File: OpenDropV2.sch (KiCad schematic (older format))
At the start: 195 parts, among them J1 DC_JACK, P1 CONN_01X01, P2 CONN_01X01, P3 CONN_01X01, P4 CONN_01X01, P5 CONN_01X01, Q1 BSS138, Q2 BSS138, Q3 BSS138, SW1 SW_PUSH, SW2 SW_PUSH, SW3 SW_PUSH, SW4 SW_PUSH, SW5 SPST, T1 IRF 840S, U1 MAX1771ESA, U2 HV507, U3 ARDUINO_MICRO, U4 HV507, U5 ESP8266_SMD

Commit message: started with corrections for V2.1
work in progress
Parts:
- C6: footprint Resistors_SMD:R_2512 -> GaudiLabsFootPrints:C100n_250V
- D1: footprint Diodes_SMD:DO-214AB -> GaudiLabsFootPrints:DO-214AA
- POT1: symbol POT -> POT-RESCUE-OpenDropV2
- U1: footprint SMD_Packages:SOIC-8-N -> GaudiLabsFootPrints:SO08
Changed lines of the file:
@@
 EESchema Schematic File Version 2
-LIBS:GaudiLabsPartsLibrary
+LIBS:OpenDropV2-rescue
 LIBS:power
 LIBS:device
@@
 LIBS:contrib
 LIBS:valves
+LIBS:GaudiLabsPartsLibrary
 LIBS:arduino_micro_shield
 LIBS:OpenDropV2-cache
@@
 F 0 "U1" H 10700 3600 50  0000 L CNN
 F 1 "MAX1771ESA" H 11150 3600 50  0000 L CNN
-F 2 "SMD_Packages:SOIC-8-N" H 11050 3200 50  0000 C CIN
+F 2 "GaudiLabsFootPrints:SO08" H 11050 3200 50  0000 C CIN
 F 3 "" H 11050 3200 60  0000 C CNN
 	1    11050 3200
@@
 F 0 "D1" H 12400 2250 50  0000 C CNN
 F 1 "ES2F" H 12400 2550 50  0000 C CNN
-F 2 "Diodes_SMD:DO-214AB" H 12400 2400 60  0001 C CNN
+F 2 "GaudiLabsFootPrints:DO-214AA" H 12400 2400 60  0001 C CNN
 F 3 "" H 12400 2400 60  0000 C CNN
 	1    12400 2400
@@
 $EndComp
 $Comp
-L POT POT1
+L POT-RESCUE-OpenDropV2 POT1
 U 1 1 55E8825C
 P 13250 3450
@@
 F 3 "" H 13250 3450 60  0000 C CNN
 	1    13250 3450
-	0    1    1    0
+	0    1    -1   0
 $EndComp
 $Comp
@@
 F 0 "C6" H 13675 3300 50  0000 L CNN
 F 1 "100nF, 250V" V 13500 3000 50  0000 L CNN
-F 2 "Resistors_SMD:R_2512" H 13688 3050 30  0001 C CNN
+F 2 "GaudiLabsFootPrints:C100n_250V" H 13688 3050 30  0001 C CNN
 F 3 "" H 13650 3200 60  0000 C CNN
 	1    13650 3200
@@
 2E 95 62 1C D3 0C 81 40 A6 05 87 C3 66 30 DE CB 45 7A 2F 79 14 02 81 CC 1D 70 1A 09 81 38 08 28
 36 08 C4 41 40 B1 41 20 0E 02 8A 0D 02 71 10 FF 3F 71 F6 E5 00 6E 12 D7 40 00 00 00 00 49 45 4E
-44 AE 42 60 82 03
+44 AE 42 60 82 32
 EndData
 $EndBitmap

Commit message: More modifications and corrections for Version 2.1
work in progress
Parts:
- removed LED6, LED7: LED, GaudiLabsFootPrints:LED_SIDE, symbol LED
- removed SW3, SW4: SW_PUSH, Buttons_Switches_SMD:SW_SPST_PTS645, symbol SW_PUSH
- added JS1: JoystickSMD, GaudiLabsFootPrints:JoystickSMD_SKQUSeries, symbol JoystickSMD
- added P6: CONN_01X30, GaudiLabsFootPrints:OLED_SolderPads, symbol CONN_01X30
- added R18, R19, R20, R21: 10k, Resistors_SMD:R_0805, symbol R
- FLUXL1, FLUXL10, FLUXL100, FLUXL101, FLUXL102, FLUXL103, FLUXL104, FLUXL105, FLUXL106, FLUXL107, FLUXL108, FLUXL109, FLUXL11, FLUXL110, FLUXL111, FLUXL112, FLUXL113, FLUXL114, FLUXL115, FLUXL116, FLUXL117, FLUXL118, FLUXL119, FLUXL12, FLUXL120, FLUXL121, FLUXL122, FLUXL123, FLUXL124, FLUXL125, FLUXL126, FLUXL127, FLUXL128, FLUXL13, FLUXL14, FLUXL15, FLUXL16, FLUXL17, FLUXL18, FLUXL19, FLUXL2, FLUXL20, FLUXL21, FLUXL22, FLUXL23, FLUXL24, FLUXL25, FLUXL26, FLUXL27, FLUXL28, FLUXL29, FLUXL3, FLUXL30, FLUXL31, FLUXL32, FLUXL33, FLUXL34, FLUXL35, FLUXL36, FLUXL37, FLUXL38, FLUXL39, FLUXL4, FLUXL40, FLUXL41, FLUXL42, FLUXL43, FLUXL44, FLUXL45, FLUXL46, FLUXL47, FLUXL48, FLUXL49, FLUXL5, FLUXL50, FLUXL51, FLUXL52, FLUXL53, FLUXL54, FLUXL55, FLUXL56, FLUXL57, FLUXL58, FLUXL59, FLUXL6, FLUXL60, FLUXL61, FLUXL62, FLUXL63, FLUXL64, FLUXL65, FLUXL66, FLUXL67, FLUXL68, FLUXL69, FLUXL7, FLUXL70, FLUXL71, FLUXL72, FLUXL73, FLUXL74, FLUXL75, FLUXL76, FLUXL77, FLUXL78, FLUXL79, FLUXL8, FLUXL80, FLUXL81, FLUXL82, FLUXL83, FLUXL84, FLUXL85, FLUXL86, FLUXL87, FLUXL88, FLUXL89, FLUXL9, FLUXL90, FLUXL91, FLUXL92, FLUXL93, FLUXL94, FLUXL95, FLUXL96, FLUXL97, FLUXL98, FLUXL99: footprint GaudiLabsFootPrints:FLUXL_PAD_2_75 -> GaudiLabsFootPrints:FLUXPAD_2_75_4MIL_4_5
- SW1, SW2: footprint Buttons_Switches_SMD:SW_SPST_PTS645 -> GaudiLabsFootPrints:PUSH_BUTTON_SMD
- U2, U4: footprint Housings_QFP:PQFP-80_14x20mm_Pitch0.8mm -> GaudiLabsFootPrints:PQFP-80_14x20mm_Pitch0.8mm
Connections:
- net +5V: now also U2.30 (POL), U4.30 (POL), R18.2; no longer U2.29 (BL), U4.29 (BL)
- net 3.3V: now also P6.6 (P6), P6.9 (P9)
- net GND: now also JS1.4 (Common), P6.10 (P10), P6.11 (P11), P6.12 (P12), P6.16 (P16), P6.17 (P17), P6.21 (P21), P6.22 (P22), P6.23 (P23), P6.24 (P24), P6.25 (P25), P6.29 (P29), P6.30 (P30), P6.8 (P8)
- net SW3: now also JS1.6 (Center)
- net at D2.2 (A), R11.2, S1.13 (CS): now also P6.13 (P13)
- net at D3.2 (A), R10.2, S1.14 (RES): now also P6.14 (P14)
- net at D4.2 (A), R14.2, S1.15 (D/C#_SA0): now also P6.15 (P15)
- net at Q1.2 (S), R13.2, S1.18 (D0_(SCL)): now also P6.18 (P18)
- net at Q2.2 (S), R12.2, S1.19 (D1_(SA)): now also P6.19 (P19)
- net at C7.1, S1.2 (C2P): now also P6.2 (P2)
- net at R3.1, S1.26 (REF): now also P6.26 (P26)
- net at C10.1, S1.27 (VCOMH): now also P6.27 (P27)
- net at C8.1, S1.28 (VCC): now also P6.28 (P28)
- net at C7.2, S1.3 (C2N): now also P6.3 (P3)
- net at C9.1, S1.4 (C1P): now also P6.4 (P4)
- net at C9.2, S1.5 (C1N): now also P6.5 (P5)
- net at U4.39 (DIO_B): now also U2.26 (DIO_A)
- net DI1 renamed DI
- net DI2: no longer names the net of U3.7 (2/SDA)
- net DI2: no longer U2.26 (DIO_A)
- removed net POL: U2.30 (POL), U3.8 (3(PWM)/SCL), U4.30 (POL)
- net SW4 renamed JOY
- net JOY: now also JS1.5 (D_(rigth)), R18.1, R19.2
- new net: JS1.1 (A_(up)), R21.1
- new net: JS1.2 (B_(left)), R20.1, R21.2
- new net: JS1.3 (C_(down)), R19.1, R20.2
- new net BL: U2.29 (BL), U3.8 (3(PWM)/SCL), U4.29 (BL)
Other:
- moved on the sheet: S1

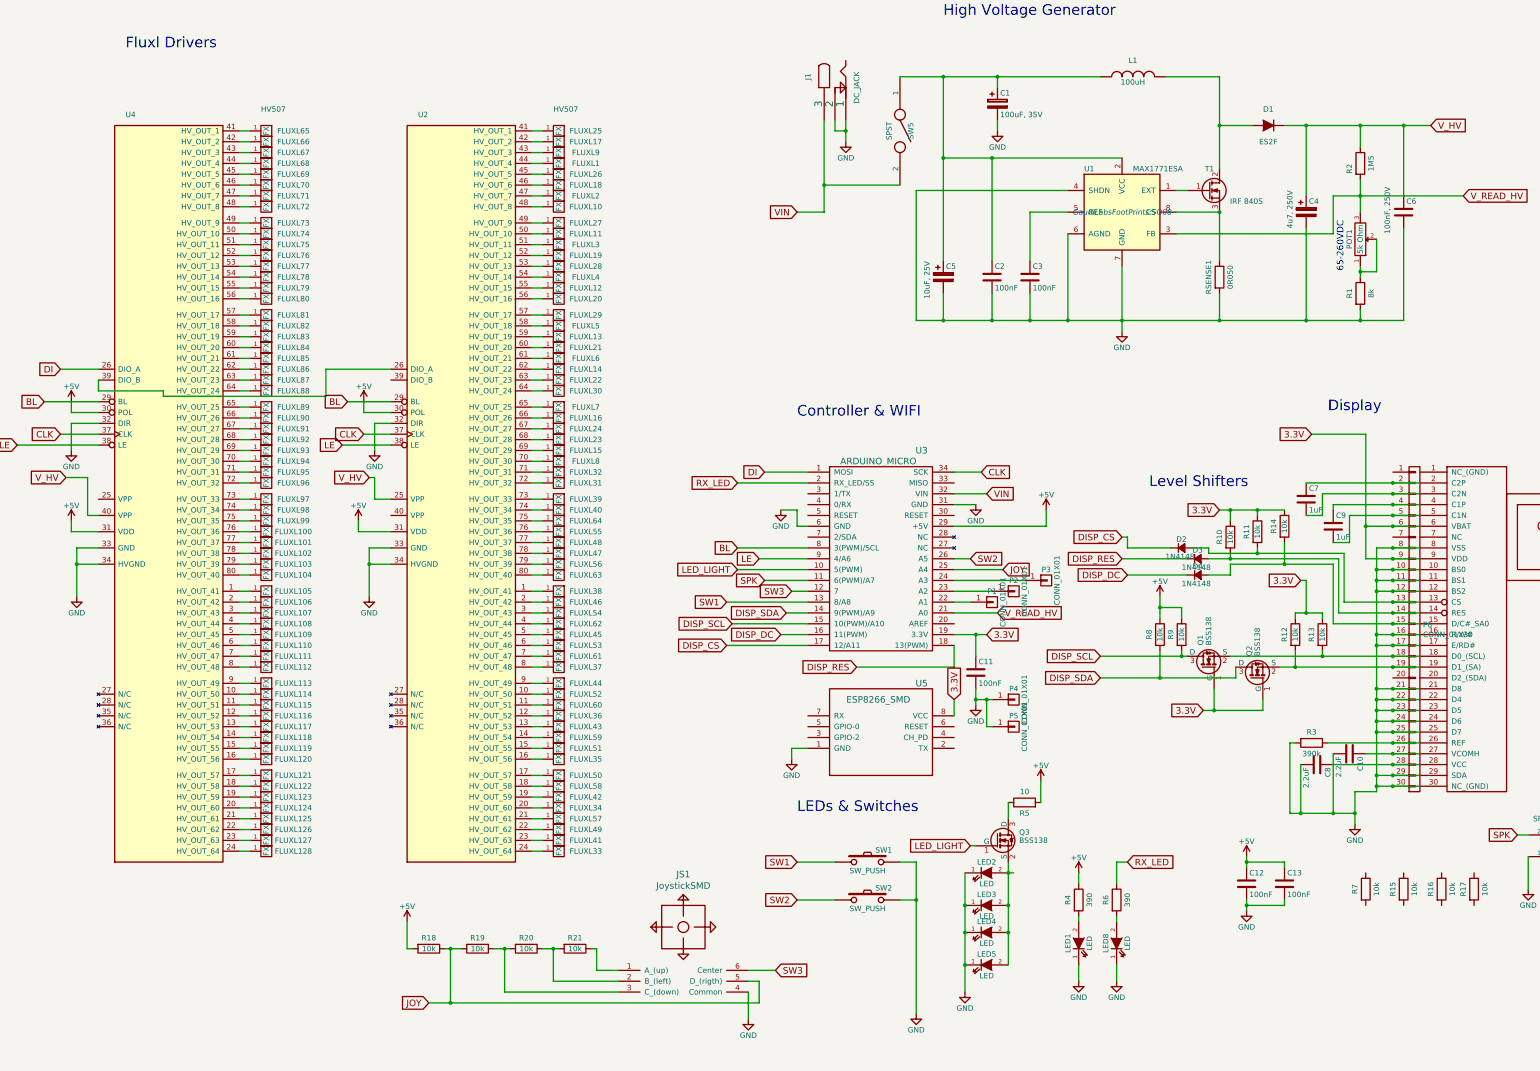
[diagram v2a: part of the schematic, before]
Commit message: added interfacing for esp-01 module, moved sda/scl, removed p3, moved BL
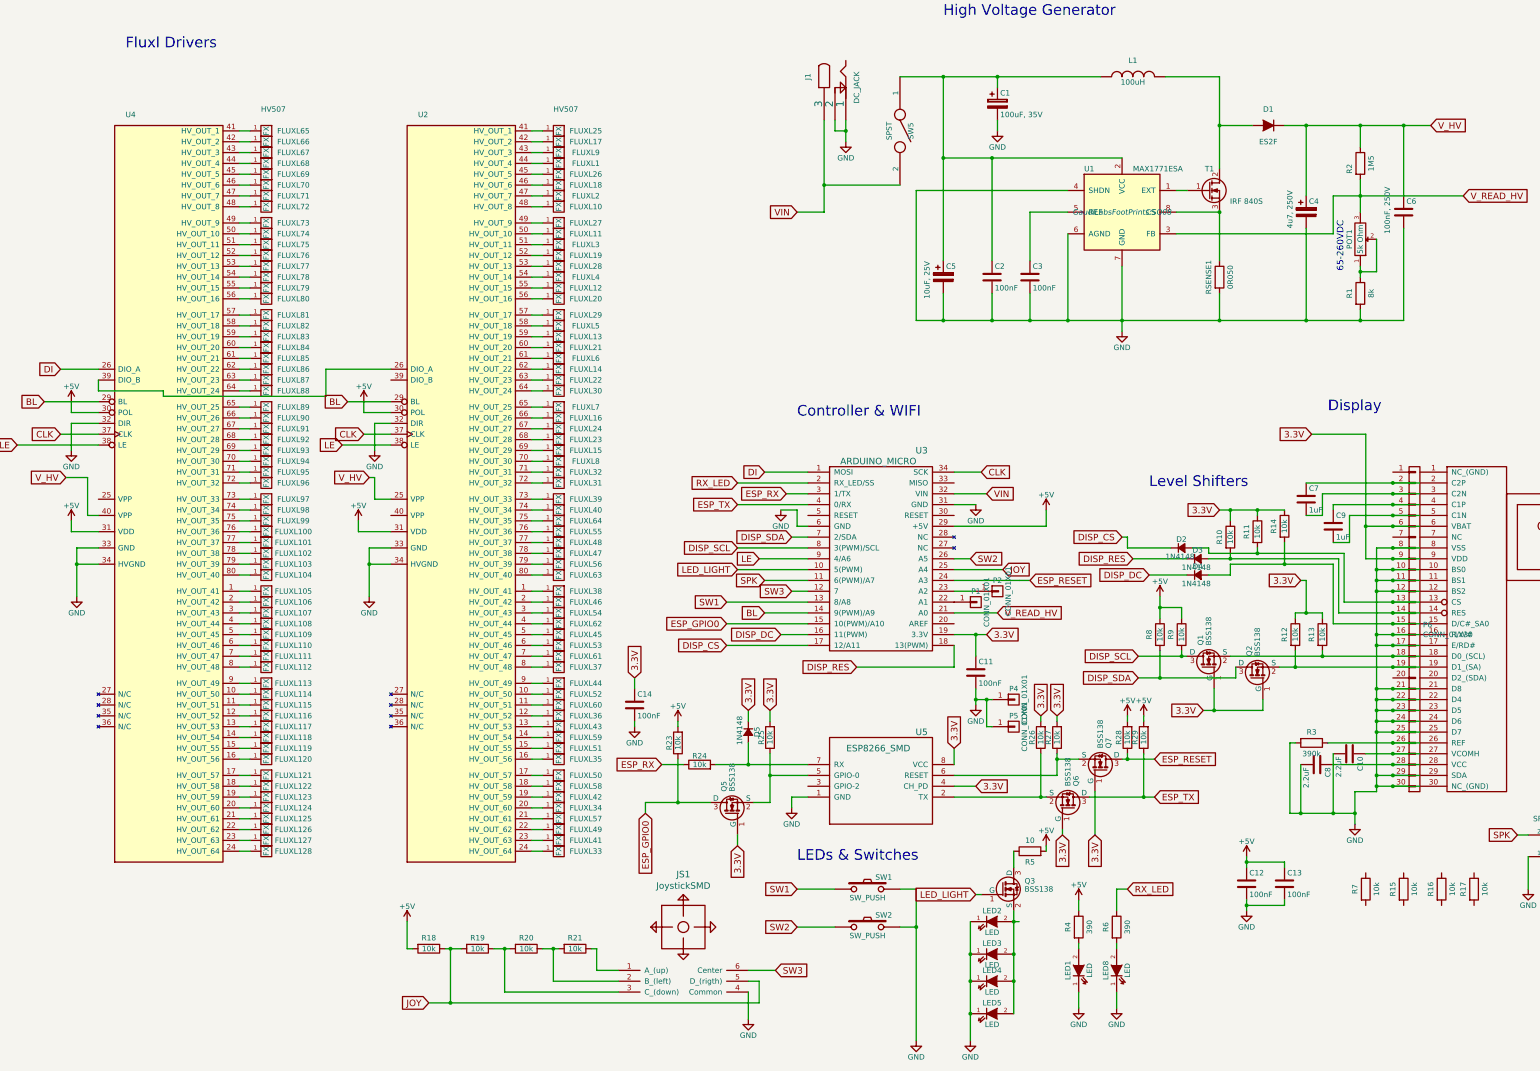
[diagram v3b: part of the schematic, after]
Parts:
- removed P3: CONN_01X01, Measurement_Points:Measurement_Point_Square-SMD-Pad_Small, symbol CONN_01X01
- added C14: 100nF, Capacitors_SMD:C_0805, symbol C
- added D5: 1N4148, Diodes_SMD:SOD-323, symbol D_Small
- added Q5, Q6, Q7: BSS138, TO_SOT_Packages_SMD:SOT-23, symbol BSS138
- added R23, R24, R25, R26, R27, R28, R29: 10k, symbol R
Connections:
- net +5V: now also R23.2, R28.2, R29.2
- net 3.3V: now also U5.4 (CH_PD), C14.1, D5.1 (K), Q5.1 (G), Q6.1 (G), Q7.1 (G), R25.2, R26.2, R27.2
- net BL: now also U3.14 (9(PWM)/A9); no longer U3.8 (3(PWM)/SCL)
- net DISP_SCL: now also U3.8 (3(PWM)/SCL); no longer U3.15 (10(PWM)/A10)
- net DISP_SDA: now also U3.7 (2/SDA); no longer U3.14 (9(PWM)/A9)
- net GND: now also C14.2
- net ESP_RESET: now reaches U3.24 (A3)
- net ESP_RESET: now also Q7.3 (D), R28.1
- net ESP_RX: now reaches U3.3 (1/TX)
- net ESP_RX: now also R24.1
- net ESP_TX: now reaches U3.4 (0/RX)
- net ESP_TX: now also Q6.3 (D), R29.1
- net at U5.2 (TX): now also Q6.2 (S), R26.1
- net at U5.5 (GPIO-0): now also Q5.2 (S), R25.1
- net at U5.6 (RESET): now also Q7.2 (S), R27.1
- net at U5.7 (RX): now also D5.2 (A), R24.2
- new net ESP_GPIO0: Q5.3 (D), R23.1, U3.15 (10(PWM)/A10)
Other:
- moved on the sheet: LED1, LED2, LED3, LED4, LED5, LED8, P1, P2, Q3, R4, R5, R6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

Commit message: Production Version of V2.1
Hopefully...
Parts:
- removed P4: CONN_01X01, Measurement_Points:Measurement_Point_Square-SMD-Pad_Small, symbol CONN_01X01
- added C15, C16, C17: 1uF, Capacitors_SMD:C_0805, symbol C
- added P10, P11, P12, P3, P7, P8, P9: CONN_01X01, Measurement_Points:Measurement_Point_Square-SMD-Pad_Small, symbol CONN_01X01
- added P13: ScrewPad1, GaudiLabsFootPrints:MountingHolePad_3x9mm, symbol CONN_01X01
- added P14: ScrewPad2, GaudiLabsFootPrints:MountingHolePad_3x9mm, symbol CONN_01X01
- added P15: ScrewPad3, GaudiLabsFootPrints:MountingHolePad_3x9mm, symbol CONN_01X01
- added P16: ScrewPad4, GaudiLabsFootPrints:MountingHolePad_3x9mm, symbol CONN_01X01
- added R22, R30, R31: 10k, Resistors_SMD:R_0805, symbol R
- added U6: MCP6002, GaudiLabsFootPrints:SO08, symbol MCP6002
- R23, R24, R25, R26, R27, R28, R29: footprint (none) -> Resistors_SMD:R_0805
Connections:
- net +5V: now also C15.1, P3.1 (P1), R22.1, U6.8 (V+), U6.8 (V+)
- net BL: now also P10.1 (P1)
- net CLK: now also P11.1 (P1)
- net GND: now also C15.2, P12.1 (P1), R30.2, U6.4 (V-), U6.4 (V-)
- net LE: now also P8.1 (P1)
- net V_HV: now also P7.1 (P1)
- net V_READ_HV: no longer POT1.3, R2.2, U1.3 (FB)
- net DIO_B: now reaches U2.39 (DIO_B)
- net DIO_B: now also P9.1 (P1)
- net at U3.22 (A1): now also P2.1 (P1); no longer P1.1 (P1)
- net FEEDBACK: now reaches U3.23 (A2)
- net FEEDBACK: now also C17.1, R31.1, U6.1; no longer P2.1 (P1)
- new net: POT1.3, R2.2, U1.3 (FB)
- new net: C16.1, C17.2, R31.2, U6.2 (-)
- new net: U6.3 (+), U6.6 (-), U6.7
- new net: R22.2, R30.1, U6.5 (+)
- new net V_GND: C16.2, P1.1 (P1), P13.1 (P1)
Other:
- moved on the sheet: C1, C2, C3, C4, C5, C6, D1, J1, L1, P2, P5, POT1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

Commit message: Production Version 2.1 with Gerber Files
Version Bittie
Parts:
- C17: value 1uF -> 1pF
- R31: value 10k -> 200k
- U5: symbol ESP8266_SMD -> ESP8266_SMD-RESCUE-OpenDropV2
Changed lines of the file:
@@
 2E 95 62 1C D3 0C 81 40 A6 05 87 C3 66 30 DE CB 45 7A 2F 79 14 02 81 CC 1D 70 1A 09 81 38 08 28
 36 08 C4 41 40 B1 41 20 0E 02 8A 0D 02 71 10 FF 3F 71 F6 E5 00 6E 12 D7 40 00 00 00 00 49 45 4E
-44 AE 42 60 82 04
+44 AE 42 60 82 D9
 EndData
 $EndBitmap
@@
 $EndComp
 $Comp
-L ESP8266_SMD U5
+L ESP8266_SMD-RESCUE-OpenDropV2 U5
 U 1 1 560143EE
 P 8850 8500
@@
 P 10050 4850
 F 0 "R31" V 9950 4850 50  0000 C CNN
-F 1 "10k" V 10050 4850 50  0000 C CNN
+F 1 "200k" V 10050 4850 50  0000 C CNN
 F 2 "Resistors_SMD:R_0805" V 9980 4850 30  0001 C CNN
 F 3 "" H 10050 4850 30  0000 C CNN
@@
 P 10050 5050
 F 0 "C17" H 10075 5150 50  0000 L CNN
-F 1 "1uF" H 10075 4950 50  0000 L CNN
+F 1 "1pF" H 10075 4950 50  0000 L CNN
 F 2 "Capacitors_SMD:C_0805" H 10088 4900 30  0001 C CNN
 F 3 "" H 10050 5050 60  0000 C CNN
